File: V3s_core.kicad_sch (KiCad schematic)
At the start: 55 parts, among them SW1 SW_Push, U1 MKDV4GCL-AB, U2 V3S-ALLWINNER, Y1 Crystal, Y2 Crystal_GND24_Small

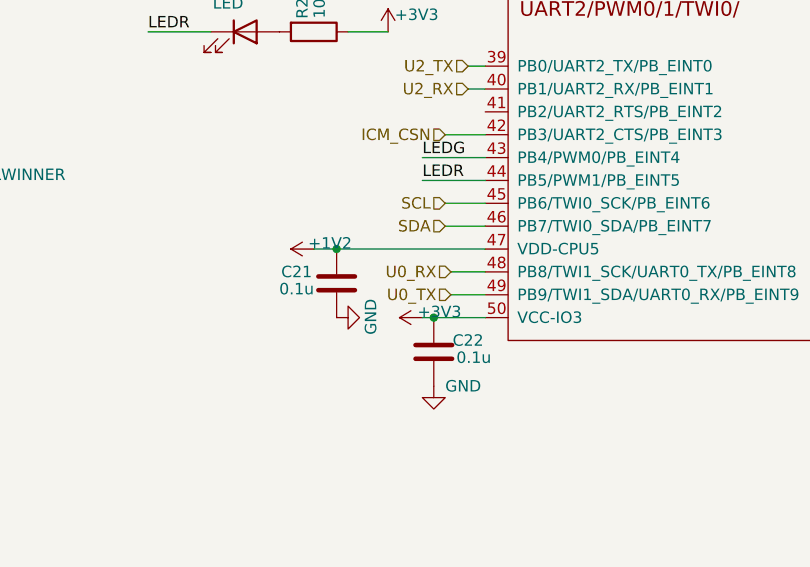
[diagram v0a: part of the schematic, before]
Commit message: fix u0_rx u0_tx wrong connection issue, fix the hole in V3s GND PAD is too small issue. update to V0.95.
Signed-off-by: ncerzzk <huangzzk@bupt.edu.cn>
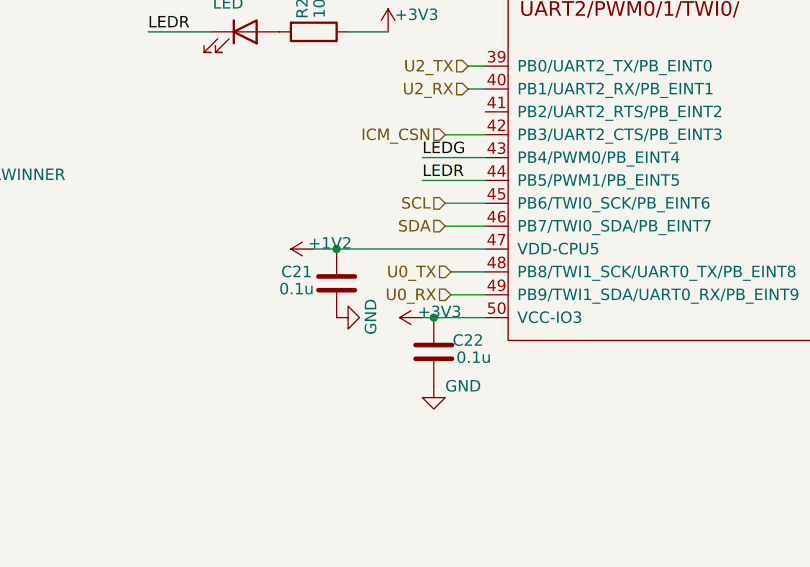
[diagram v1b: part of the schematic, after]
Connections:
- net U0_RX: now also U2.49 (PB9/TWI1_SDA/UART0_RX/PB_EINT9); no longer U2.48 (PB8/TWI1_SCK/UART0_TX/PB_EINT8)
- net U0_TX: now also U2.48 (PB8/TWI1_SCK/UART0_TX/PB_EINT8); no longer U2.49 (PB9/TWI1_SDA/UART0_RX/PB_EINT9)
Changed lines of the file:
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@@
-    (effects (font (size 1.27 1.27)) (justify right))
-  )
-  (hierarchical_label "U0_TX" (shape input) (at 237.49 89.535 180)
     (effects (font (size 1.27 1.27)) (justify right))
   )
@@
     (effects (font (size 1.27 1.27)) (justify right))
   )
-  (hierarchical_label "U0_RX" (shape input) (at 237.49 86.995 180)
+  (hierarchical_label "U2_TX" (shape input) (at 239.395 64.135 180)
     (effects (font (size 1.27 1.27)) (justify right))
   )
-  (hierarchical_label "U2_TX" (shape input) (at 239.395 64.135 180)
+  (hierarchical_label "U0_TX" (shape input) (at 237.49 86.995 180)
     (effects (font (size 1.27 1.27)) (justify right))
   )
@@
     (effects (font (size 1.27 1.27)) (justify right))
   )
+  (hierarchical_label "U0_RX" (shape input) (at 237.49 89.535 180)
+    (effects (font (size 1.27 1.27)) (justify right))
+  )

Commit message: use LDO to produce 1.2V, to fix fpga voltage issue. fix wrong fpga sch issue, change the pins of fpga. connect fpga SSPI to V3s-spi, so that we can configuare fpag on v3s someday.
Signed-off-by: ncerzzk <huangzzk@bupt.edu.cn>
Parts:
- Y2: footprint Crystal:Crystal_SMD_EuroQuartz_MT-4Pin_3.2x2.5mm_HandSoldering -> Crystal:Crystal_SMD_EuroQuartz_MT-4Pin_3.2x2.5mm
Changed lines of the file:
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@@
       (effects (font (size 1.27 1.27)) hide)
     )
-    (property "Footprint" "Crystal:Crystal_SMD_EuroQuartz_MT-4Pin_3.2x2.5mm_HandSoldering" (id 2) (at 205.486 225.298 0)
+    (property "Footprint" "Crystal:Crystal_SMD_EuroQuartz_MT-4Pin_3.2x2.5mm" (id 2) (at 205.486 225.298 0)
       (effects (font (size 1.27 1.27)) hide)
     )

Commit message: v1.0
Signed-off-by: ncerzzk <huangzzk@bupt.edu.cn>
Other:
- note added: "NC"
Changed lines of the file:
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@@
     (stroke (width 0) (type default) (color 0 0 0 0))
+  )
+  (text "NC" (at 26.035 245.11 0)
+    (effects (font (size 1.27 1.27)) (justify left bottom))
+  )
+  (text "NC" (at 214.63 58.42 0)
+    (effects (font (size 1.27 1.27)) (justify left bottom))
+  )
+  (text "NC" (at 214.63 51.435 0)
+    (effects (font (size 1.27 1.27)) (justify left bottom))
   )
   (label "SD_CMD" (at 43.18 211.455 0)
@@
   )
   (symbol (lib_id "Switch:SW_Push") (at 27.305 241.935 0) (unit 1)
-    (in_bom yes) (on_board yes) (fields_autoplaced)
-    (property "Reference" "SW1" (id 0) (at 27.305 233.68 0))
-    (property "Value" "SW_Push" (id 1) (at 27.305 236.22 0))
+    (in_bom yes) (on_board yes)
+    (property "Reference" "SW1" (id 0) (at 27.305 234.95 0))
+    (property "Value" "SW_Push" (id 1) (at 27.305 236.855 0))
     (property "Footprint" "Button_Switch_SMD:SW_Push_SPST_NO_Alps_SKRK" (id 2) (at 27.305 236.855 0)
       (effects (font (size 1.27 1.27)) hide)

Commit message: update 2.0
Signed-off-by: huangzzk <huangcmzzk@gmail.com>
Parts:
- removed D2, D3: LED, LED_SMD:LED_0603_1608Metric, symbol Device:LED
- removed R25, R26: 10K, Resistor_SMD:R_0402_1005Metric, symbol Device:R
- removed R27: 499R, Resistor_SMD:R_0402_1005Metric, symbol Device:R
- removed SW1: SW_Push, Button_Switch_SMD:SW_Push_SPST_NO_Alps_SKRK, symbol Switch:SW_Push
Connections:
- net LEDG: now also U2.13 (PE18/CSI_D14/LCD_D20); no longer U2.43 (PB4/PWM0/PB_EINT4)
- net LEDR: now also U2.14 (PE17/CSI_D13/LCD_D19); no longer U2.44 (PB5/PWM1/PB_EINT5)
- net USER_CSN2: now reaches U2.11 (PE19/CSI_D15/LCD_D21)
- net GPIO_EXT12: now reaches U2.22 (PE12/CSI_D8/LCD_D12)
- net GPIO_EXT11: now reaches U2.23 (PE11/CSI_D7/LCD_D11)
- net GPIO_EXT10: now reaches U2.24 (PE10/CSI_D6/LCD_D10)
- net GPIO_EXT9: now reaches U2.27 (PE9/CSI_D5/LCD_D7)
- net GPIO_EXT8: now reaches U2.28 (PE8/CSI_D4/LCD_D6)
- net GPIO_EXT7: now reaches U2.30 (PE7/CSI_D3/LCD_D5)
- net GPIO_EXT6: now reaches U2.31 (PE6/CSI_D2/LCD_D4)
- net GPIO_EXT5: now reaches U2.32 (PE5/CSI_D1/LCD_D3)
- net GPIO_EXT4: now reaches U2.33 (PE4/CSI_D0/LCD_D2)
- net GPIO_EXT3: now reaches U2.34 (PE3/CSI_VSYNC/LCD_VSYNC)
- net GPIO_EXT2: now reaches U2.35 (PE2/CSI_HSYNC/LCD_HSYNC)
- net GPIO_EXT1: now reaches U2.36 (PE1/CSI_MCLK/LCD_DE)
- net GPIO_EXT0: now reaches U2.37 (PE0/CSI_PCLK/LCD_CLK)
- net GPIO_EXT13: now reaches U2.6 (PE24/LCD_D23)
- net CS renamed USER_CS1
- new net PWM_OUT: U2.43 (PB4/PWM0/PB_EINT4)
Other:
- note removed: "NC"
- moved on the sheet: C3, C5, C7
